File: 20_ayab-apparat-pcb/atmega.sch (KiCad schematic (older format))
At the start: 36 parts, among them P7 CONN_3X2, P8 CONN_4, P9 CONN_2, SW1 SW_PUSH, U6 ATMEGA32U4-A, U8 BLM21, X1 16MHz, X2 USBMICRO

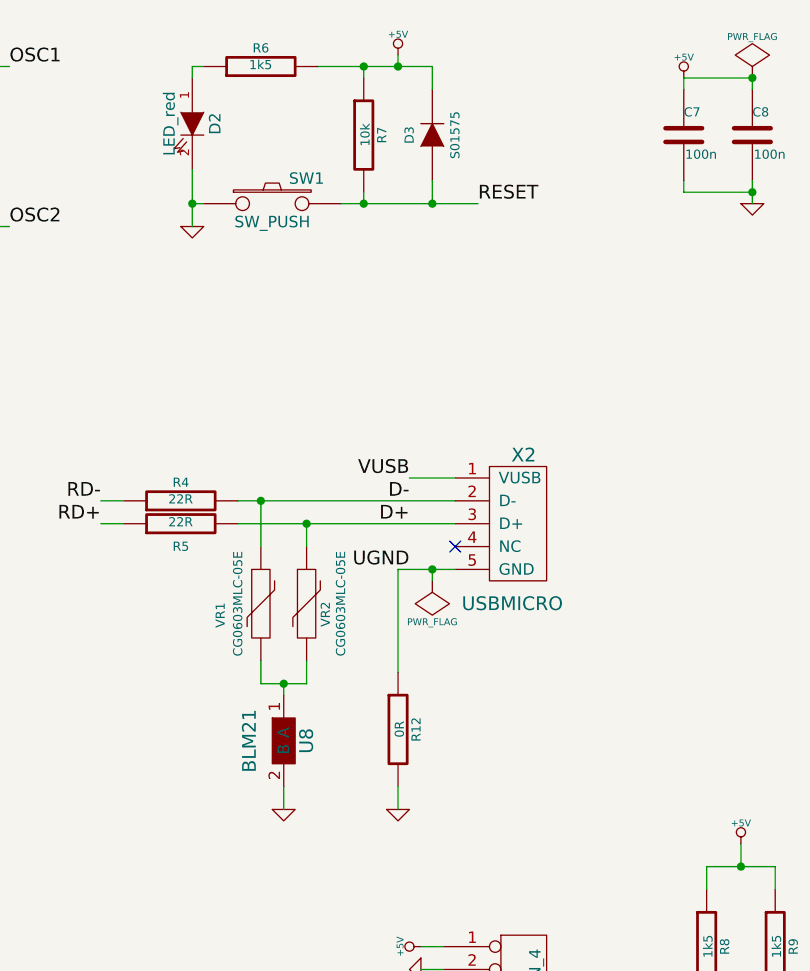
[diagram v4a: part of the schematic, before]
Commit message: BOM nearly done TODO add relais for autoswitch when USB 5V is connected to schematic
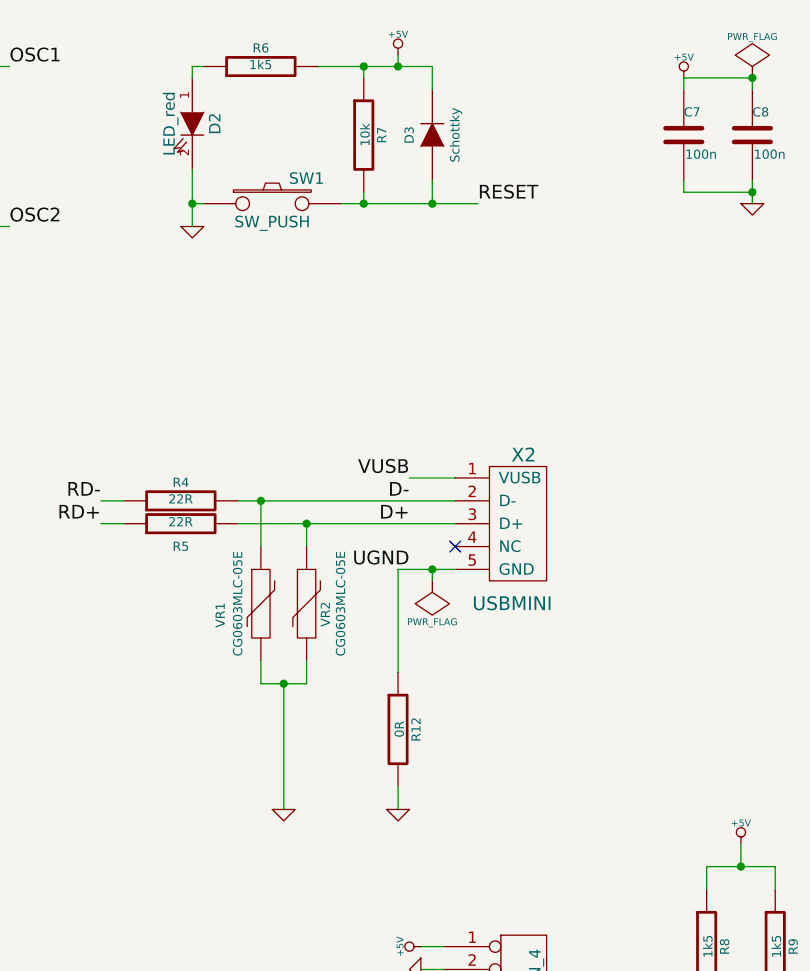
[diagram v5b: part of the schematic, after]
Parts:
- removed U8: BLM21, symbol FERRITE
- D3: value S01575 -> Schottky
- X2: value USBMICRO -> USBMINI
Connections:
- net GND: now also VR1.2, VR2.2
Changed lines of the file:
@@
 OSC2
 $Comp
-L GND #PWR034
+L GND #PWR033
 U 1 1 52E8074E
 P 4750 1850
-F 0 "#PWR034" H 4750 1850 30  0001 C CNN
+F 0 "#PWR033" H 4750 1850 30  0001 C CNN
 F 1 "GND" H 4750 1780 30  0001 C CNN
 F 2 "" H 4750 1850 60  0000 C CNN
@@
 $EndComp
 $Comp
-L PWR_FLAG #FLG035
+L PWR_FLAG #FLG034
 U 1 1 52E8077D
 P 4750 1100
-F 0 "#FLG035" H 4750 1195 30  0001 C CNN
+F 0 "#FLG034" H 4750 1195 30  0001 C CNN
 F 1 "PWR_FLAG" H 4750 1280 30  0000 C CNN
 F 2 "" H 4750 1100 60  0000 C CNN
@@
 $EndComp
 $Comp
-L GND #PWR036
+L GND #PWR035
 U 1 1 52E80927
 P 9200 1700
-F 0 "#PWR036" H 9200 1700 30  0001 C CNN
+F 0 "#PWR035" H 9200 1700 30  0001 C CNN
 F 1 "GND" H 9200 1630 30  0001 C CNN
 F 2 "" H 9200 1700 60  0000 C CNN
@@
 $EndComp
 $Comp
-L +5V #PWR037
+L +5V #PWR036
 U 1 1 52E8098A
 P 2650 2450
-F 0 "#PWR037" H 2650 2540 20  0001 C CNN
+F 0 "#PWR036" H 2650 2540 20  0001 C CNN
 F 1 "+5V" H 2650 2540 30  0000 C CNN
 F 2 "" H 2650 2450 60  0000 C CNN
@@
 $EndComp
 $Comp
-L PWR_FLAG #FLG038
+L PWR_FLAG #FLG037
 U 1 1 52E809A6
 P 9200 1150
-F 0 "#FLG038" H 9200 1245 30  0001 C CNN
+F 0 "#FLG037" H 9200 1245 30  0001 C CNN
 F 1 "PWR_FLAG" H 9200 1330 30  0000 C CNN
 F 2 "" H 9200 1150 60  0000 C CNN
@@
 $EndComp
 $Comp
-L GND #PWR039
+L GND #PWR038
 U 1 1 52E80AA1
 P 1450 5850
-F 0 "#PWR039" H 1450 5850 30  0001 C CNN
+F 0 "#PWR038" H 1450 5850 30  0001 C CNN
 F 1 "GND" H 1450 5780 30  0001 C CNN
 F 2 "" H 1450 5850 60  0000 C CNN
@@
 ISP
 $Comp
-L GND #PWR040
+L GND #PWR039
 U 1 1 52E80DFA
 P 7100 5850
-F 0 "#PWR040" H 7100 5850 30  0001 C CNN
+F 0 "#PWR039" H 7100 5850 30  0001 C CNN
 F 1 "GND" H 7100 5780 30  0001 C CNN
 F 2 "" H 7100 5850 60  0000 C CNN
@@
 MOSI
 $Comp
-L +5V #PWR041
+L +5V #PWR040
 U 1 1 52E80E45
 P 7100 5600
-F 0 "#PWR041" H 7100 5690 20  0001 C CNN
+F 0 "#PWR040" H 7100 5690 20  0001 C CNN
 F 1 "+5V" H 7100 5690 30  0000 C CNN
 F 2 "" H 7100 5600 60  0000 C CNN
@@
 P 7800 1400
 F 0 "D3" H 7800 1500 40  0000 C CNN
-F 1 "S01575" H 7800 1300 40  0000 C CNN
+F 1 "Schottky" H 7800 1300 40  0000 C CNN
 F 2 "" H 7800 1400 60  0000 C CNN
 F 3 "" H 7800 1400 60  0000 C CNN
@@
 $EndComp
 $Comp
-L +5V #PWR042
+L +5V #PWR041
 U 1 1 52E8110B
 P 7650 1050
-F 0 "#PWR042" H 7650 1140 20  0001 C CNN
+F 0 "#PWR041" H 7650 1140 20  0001 C CNN
 F 1 "+5V" H 7650 1140 30  0000 C CNN
 F 2 "" H 7650 1050 60  0000 C CNN
@@
 $EndComp
 $Comp
-L GND #PWR043
+L GND #PWR042
 U 1 1 52E813A7
 P 6750 1800
-F 0 "#PWR043" H 6750 1800 30  0001 C CNN
+F 0 "#PWR042" H 6750 1800 30  0001 C CNN
 F 1 "GND" H 6750 1730 30  0001 C CNN
 F 2 "" H 6750 1800 60  0000 C CNN
@@
 $EndComp
 $Comp
-L +5V #PWR044
+L +5V #PWR043
 U 1 1 52E81906
 P 4350 3500
-F 0 "#PWR044" H 4350 3590 20  0001 C CNN
+F 0 "#PWR043" H 4350 3590 20  0001 C CNN
 F 1 "+5V" H 4350 3590 30  0000 C CNN
 F 2 "" H 4350 3500 60  0000 C CNN
@@
 $EndComp
 $Comp
-L +5V #PWR045
+L +5V #PWR044
 U 1 1 52E81C3C
 P 1300 5300
-F 0 "#PWR045" H 1300 5390 20  0001 C CNN
+F 0 "#PWR044" H 1300 5390 20  0001 C CNN
 F 1 "+5V" H 1300 5390 30  0000 C CNN
 F 2 "" H 1300 5300 60  0000 C CNN
@@
 RESET
 $Comp
-L GND #PWR046
+L GND #PWR045
 U 1 1 52E9637A
 P 2900 6200
-F 0 "#PWR046" H 2900 6200 30  0001 C CNN
+F 0 "#PWR045" H 2900 6200 30  0001 C CNN
 F 1 "GND" H 2900 6130 30  0001 C CNN
 F 2 "" H 2900 6200 60  0000 C CNN
@@
 $EndComp
 $Comp
-L GND #PWR047
+L GND #PWR046
 U 1 1 52E97A05
 P 7150 4350
-F 0 "#PWR047" H 7150 4350 30  0001 C CNN
+F 0 "#PWR046" H 7150 4350 30  0001 C CNN
 F 1 "GND" H 7150 4280 30  0001 C CNN
 F 2 "" H 7150 4350 60  0000 C CNN
@@
 $EndComp
 $Comp
-L GND #PWR048
+L GND #PWR047
 U 1 1 52E97015
 P 10050 1700
-F 0 "#PWR048" H 10050 1700 30  0001 C CNN
+F 0 "#PWR047" H 10050 1700 30  0001 C CNN
 F 1 "GND" H 10050 1630 30  0001 C CNN
 F 2 "" H 10050 1700 60  0000 C CNN
@@
 $EndComp
 $Comp
-L GND #PWR049
+L GND #PWR048
 U 1 1 52E972FE
 P 10550 1700
-F 0 "#PWR049" H 10550 1700 30  0001 C CNN
+F 0 "#PWR048" H 10550 1700 30  0001 C CNN
 F 1 "GND" H 10550 1630 30  0001 C CNN
 F 2 "" H 10550 1700 60  0000 C CNN
@@
 RXLED
 $Comp
-L +5V #PWR050
+L +5V #PWR049
 U 1 1 52E980C3
 P 10050 4500
-F 0 "#PWR050" H 10050 4590 20  0001 C CNN
+F 0 "#PWR049" H 10050 4590 20  0001 C CNN
 F 1 "+5V" H 10050 4590 30  0000 C CNN
 F 2 "" H 10050 4500 60  0000 C CNN
@@
 $EndComp
 $Comp
-L +5V #PWR051
+L +5V #PWR050
 U 1 1 52EA92E6
 P 7750 5650
-F 0 "#PWR051" H 7750 5740 20  0001 C CNN
+F 0 "#PWR050" H 7750 5740 20  0001 C CNN
 F 1 "+5V" H 7750 5740 30  0000 C CNN
 F 2 "" H 7750 5650 60  0000 C CNN
@@
 $EndComp
 $Comp
-L +5V #PWR052
+L +5V #PWR051
 U 1 1 52EA9766
 P 7750 4950
-F 0 "#PWR052" H 7750 5040 20  0001 C CNN
+F 0 "#PWR051" H 7750 5040 20  0001 C CNN
 F 1 "+5V" H 7750 5040 30  0000 C CNN
 F 2 "" H 7750 4950 60  0000 C CNN
@@
 $EndComp
 $Comp
-L GND #PWR053
+L GND #PWR052
 U 1 1 52EA977A
 P 7750 5050
-F 0 "#PWR053" H 7750 5050 30  0001 C CNN
+F 0 "#PWR052" H 7750 5050 30  0001 C CNN
 F 1 "GND" H 7750 4980 30  0001 C CNN
 F 2 "" H 7750 5050 60  0000 C CNN
@@
 LED2
 $Comp
-L +5V #PWR054
+L +5V #PWR053
 U 1 1 52EA9B0A
 P 9150 4500
-F 0 "#PWR054" H 9150 4590 20  0001 C CNN
+F 0 "#PWR053" H 9150 4590 20  0001 C CNN
 F 1 "+5V" H 9150 4590 30  0000 C CNN
 F 2 "" H 9150 4500 60  0000 C CNN
@@
 LED1
 $Comp
-L +5V #PWR055
+L +5V #PWR054
 U 1 1 52EAA0EE
 P 3050 2050
-F 0 "#PWR055" H 3050 2140 20  0001 C CNN
+F 0 "#PWR054" H 3050 2140 20  0001 C CNN
 F 1 "+5V" H 3050 2140 30  0000 C CNN
 F 2 "" H 3050 2050 60  0000 C CNN
@@
 $EndComp
 $Comp
-L +5V #PWR056
+L +5V #PWR055
 U 1 1 52EAA124
 P 8900 1150
-F 0 "#PWR056" H 8900 1240 20  0001 C CNN
+F 0 "#PWR055" H 8900 1240 20  0001 C CNN
 F 1 "+5V" H 8900 1240 30  0000 C CNN
 F 2 "" H 8900 1150 60  0000 C CNN
@@
 P 8200 3100
 F 0 "X2" H 8200 2800 60  0000 C CNN
-F 1 "USBMICRO" H 8250 3450 60  0000 C CNN
+F 1 "USBMINI" H 8250 3450 60  0000 C CNN
 F 2 "" H 8200 3100 60  0000 C CNN
 F 3 "" H 8200 3100 60  0000 C CNN
 	1    8200 3100
 	-1   0    0    1
-$EndComp
-$Comp
-L FERRITE U8
-U 1 1 52EAB329
-P 7150 4050
-F 0 "U8" V 7250 4050 60  0000 C CNN
-F 1 "BLM21" V 7000 4050 60  0000 C CNN
-F 2 "" H 7150 4050 60  0000 C CNN
-F 3 "" H 7150 4050 60  0000 C CNN
-	1    7150 4050
-	1    0    0    -1
 $EndComp
 Text Notes 4150 7500 0    60   ~ 0
@@
 NoConn ~ 7900 3200
 $Comp
-L PWR_FLAG #FLG057
+L PWR_FLAG #FLG056
 U 1 1 52EECE5F
 P 3200 2600
-F 0 "#FLG057" H 3200 2695 30  0001 C CNN
+F 0 "#FLG056" H 3200 2695 30  0001 C CNN
 F 1 "PWR_FLAG" H 3200 2780 30  0000 C CNN
 F 2 "" H 3200 2600 60  0000 C CNN
@@
 $EndComp
 $Comp
-L PWR_FLAG #FLG058
+L PWR_FLAG #FLG057
 U 1 1 52EECE74
 P 7800 3350
-F 0 "#FLG058" H 7800 3445 30  0001 C CNN
+F 0 "#FLG057" H 7800 3445 30  0001 C CNN
 F 1 "PWR_FLAG" H 7800 3530 30  0000 C CNN
 F 2 "" H 7800 3350 60  0000 C CNN
@@
 	7050 3800 7050 3700
 Wire Wire Line
-	7150 4350 7150 4250
+	7150 3800 7150 4350
 Connection ~ 7150 3800
 Connection ~ 7250 3100
@@
 Wire Wire Line
 	7900 2900 7700 2900
-Wire Wire Line
-	7150 3800 7150 3850
 Wire Wire Line
 	3000 2600 3000 2700
@@
 	7650 3750 7650 3300
 $Comp
-L GND #PWR059
+L GND #PWR058
 U 1 1 52F17DE8
 P 7650 4350
-F 0 "#PWR059" H 7650 4350 30  0001 C CNN
+F 0 "#PWR058" H 7650 4350 30  0001 C CNN
 F 1 "GND" H 7650 4280 30  0001 C CNN
 F 2 "" H 7650 4350 60  0000 C CNN

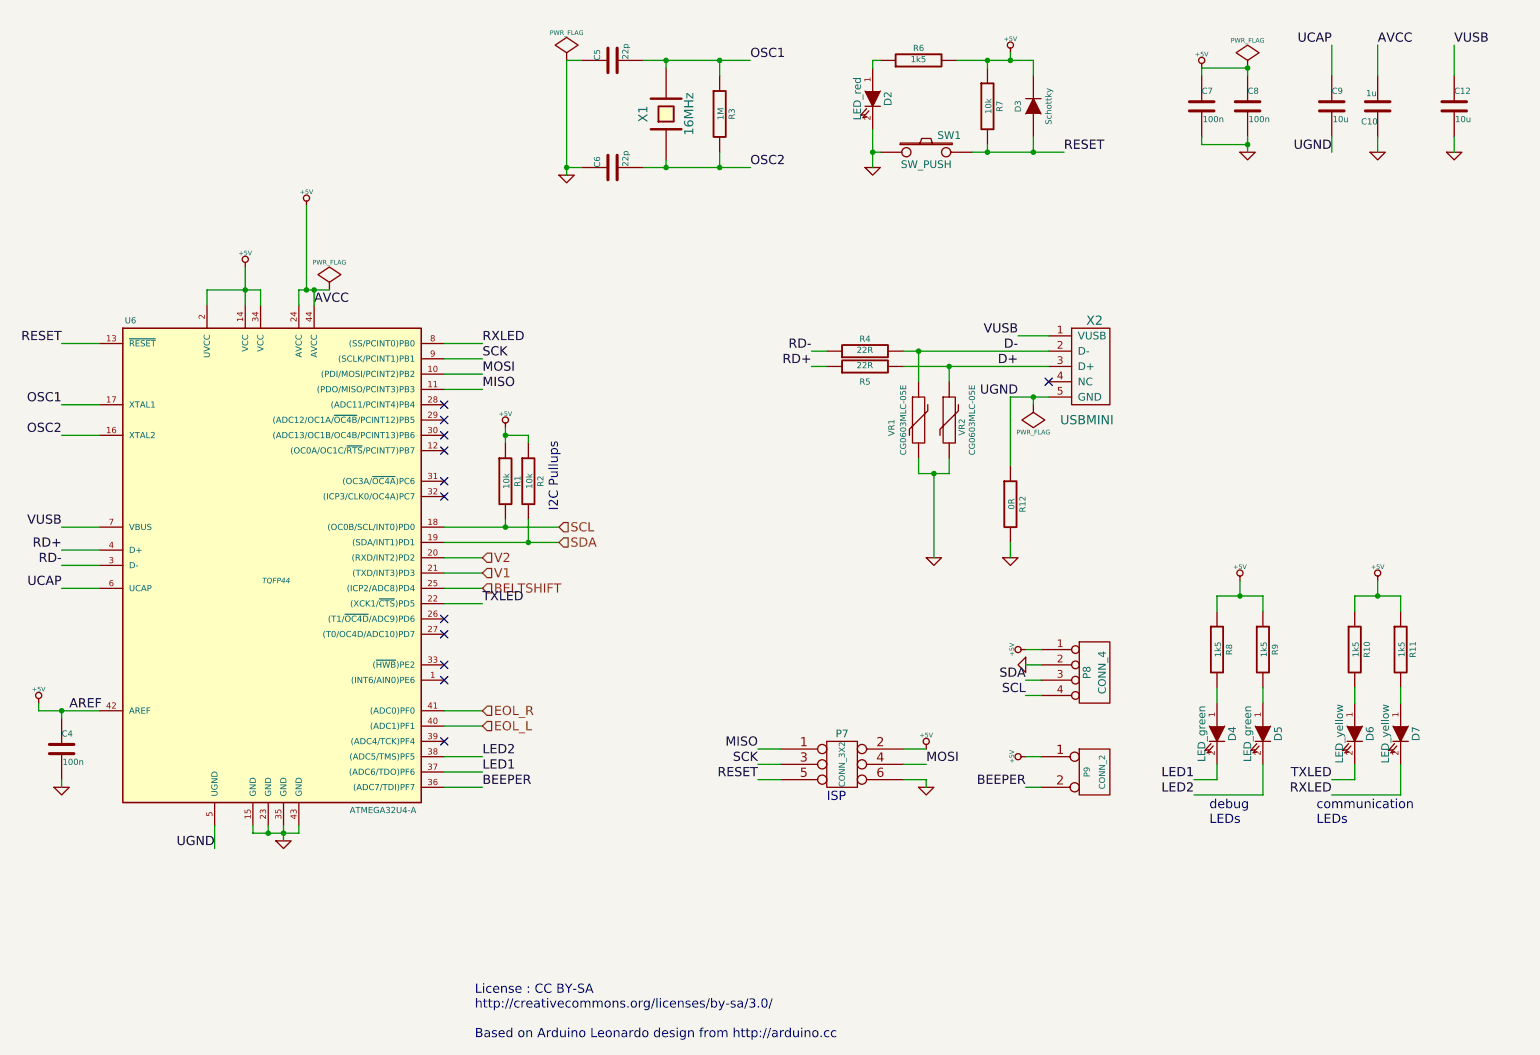
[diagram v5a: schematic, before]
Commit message: Added automatic switching between ATmega and original machine control when VUSB is attached
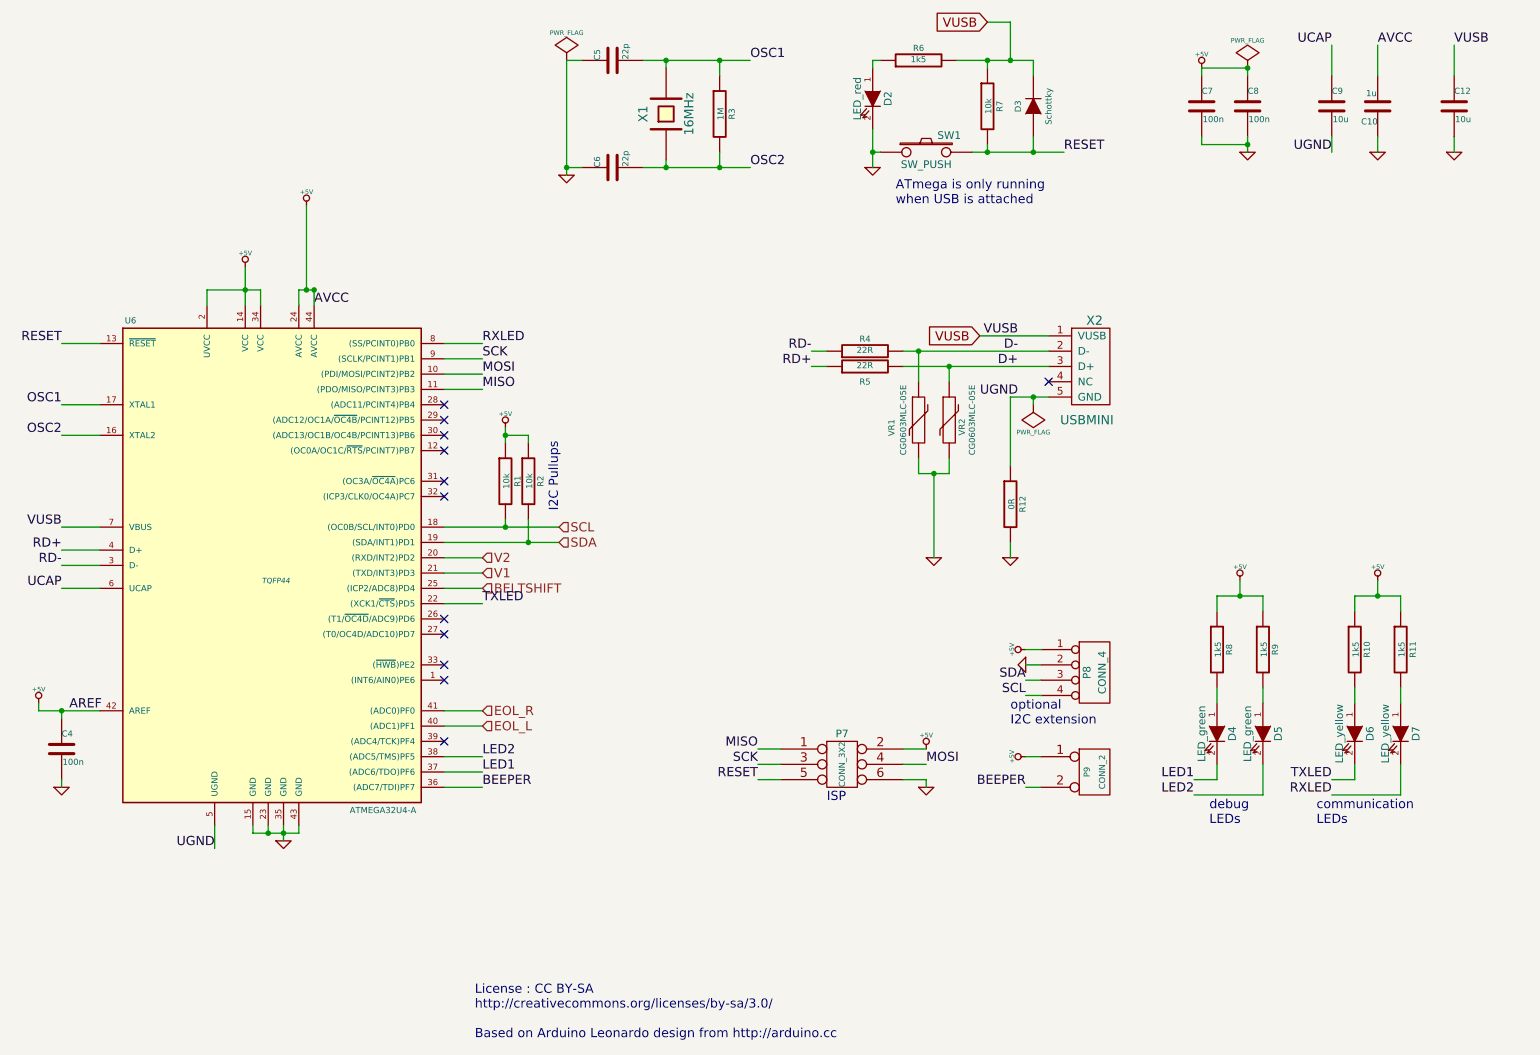
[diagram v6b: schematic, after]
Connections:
- net +5V: no longer D3.2 (K), R6.2, R7.1
- net VUSB: now also D3.2 (K), R6.2, R7.1
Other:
- note added: "ATmega is only running\nwhen USB is attached"
- note added: "optional\nI2C extension"
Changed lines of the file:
@@
 OSC2
 $Comp
-L GND #PWR033
+L GND #PWR034
 U 1 1 52E8074E
 P 4750 1850
-F 0 "#PWR033" H 4750 1850 30  0001 C CNN
+F 0 "#PWR034" H 4750 1850 30  0001 C CNN
 F 1 "GND" H 4750 1780 30  0001 C CNN
 F 2 "" H 4750 1850 60  0000 C CNN
@@
 $EndComp
 $Comp
-L PWR_FLAG #FLG034
+L PWR_FLAG #FLG035
 U 1 1 52E8077D
 P 4750 1100
-F 0 "#FLG034" H 4750 1195 30  0001 C CNN
+F 0 "#FLG035" H 4750 1195 30  0001 C CNN
 F 1 "PWR_FLAG" H 4750 1280 30  0000 C CNN
 F 2 "" H 4750 1100 60  0000 C CNN
@@
 $EndComp
 $Comp
-L GND #PWR035
+L GND #PWR036
 U 1 1 52E80927
 P 9200 1700
-F 0 "#PWR035" H 9200 1700 30  0001 C CNN
+F 0 "#PWR036" H 9200 1700 30  0001 C CNN
 F 1 "GND" H 9200 1630 30  0001 C CNN
 F 2 "" H 9200 1700 60  0000 C CNN
@@
 $EndComp
 $Comp
-L +5V #PWR036
+L +5V #PWR037
 U 1 1 52E8098A
 P 2650 2450
-F 0 "#PWR036" H 2650 2540 20  0001 C CNN
+F 0 "#PWR037" H 2650 2540 20  0001 C CNN
 F 1 "+5V" H 2650 2540 30  0000 C CNN
 F 2 "" H 2650 2450 60  0000 C CNN
@@
 $EndComp
 $Comp
-L PWR_FLAG #FLG037
+L PWR_FLAG #FLG038
 U 1 1 52E809A6
 P 9200 1150
-F 0 "#FLG037" H 9200 1245 30  0001 C CNN
+F 0 "#FLG038" H 9200 1245 30  0001 C CNN
 F 1 "PWR_FLAG" H 9200 1330 30  0000 C CNN
 F 2 "" H 9200 1150 60  0000 C CNN
@@
 $EndComp
 $Comp
-L GND #PWR038
+L GND #PWR039
 U 1 1 52E80AA1
 P 1450 5850
-F 0 "#PWR038" H 1450 5850 30  0001 C CNN
+F 0 "#PWR039" H 1450 5850 30  0001 C CNN
 F 1 "GND" H 1450 5780 30  0001 C CNN
 F 2 "" H 1450 5850 60  0000 C CNN
@@
 ISP
 $Comp
-L GND #PWR039
+L GND #PWR040
 U 1 1 52E80DFA
 P 7100 5850
-F 0 "#PWR039" H 7100 5850 30  0001 C CNN
+F 0 "#PWR040" H 7100 5850 30  0001 C CNN
 F 1 "GND" H 7100 5780 30  0001 C CNN
 F 2 "" H 7100 5850 60  0000 C CNN
@@
 MOSI
 $Comp
-L +5V #PWR040
+L +5V #PWR041
 U 1 1 52E80E45
 P 7100 5600
-F 0 "#PWR040" H 7100 5690 20  0001 C CNN
+F 0 "#PWR041" H 7100 5690 20  0001 C CNN
 F 1 "+5V" H 7100 5690 30  0000 C CNN
 F 2 "" H 7100 5600 60  0000 C CNN
@@
 	1    7800 1400
 	0    -1   -1   0
-$EndComp
-$Comp
-L +5V #PWR041
-U 1 1 52E8110B
-P 7650 1050
-F 0 "#PWR041" H 7650 1140 20  0001 C CNN
-F 1 "+5V" H 7650 1140 30  0000 C CNN
-F 2 "" H 7650 1050 60  0000 C CNN
-F 3 "" H 7650 1050 60  0000 C CNN
-	1    7650 1050
-	1    0    0    -1
 $EndComp
 Text Label 8000 1700 0    60   ~ 0
@@
 $Comp
 L PWR_FLAG #FLG056
-U 1 1 52EECE5F
-P 3200 2600
-F 0 "#FLG056" H 3200 2695 30  0001 C CNN
-F 1 "PWR_FLAG" H 3200 2780 30  0000 C CNN
-F 2 "" H 3200 2600 60  0000 C CNN
-F 3 "" H 3200 2600 60  0000 C CNN
-	1    3200 2600
-	1    0    0    -1
-$EndComp
-$Comp
-L PWR_FLAG #FLG057
 U 1 1 52EECE74
 P 7800 3350
-F 0 "#FLG057" H 7800 3445 30  0001 C CNN
+F 0 "#FLG056" H 7800 3445 30  0001 C CNN
 F 1 "PWR_FLAG" H 7800 3530 30  0000 C CNN
 F 2 "" H 7800 3350 60  0000 C CNN
@@
 	7800 1100 7800 1200
 Wire Wire Line
-	7650 1100 7650 1050
+	7650 850  7650 1100
 Connection ~ 7650 1100
 Wire Wire Line
@@
 	10050 1600 10050 1700
 Wire Wire Line
-	3000 2600 3200 2600
-Wire Wire Line
 	10550 1600 10550 1700
 Wire Wire Line
@@
 	9300 5900 8850 5900
 Wire Wire Line
-	7900 2900 7700 2900
+	7900 2900 7450 2900
 Wire Wire Line
 	3000 2600 3000 2700
@@
 	7650 3750 7650 3300
 $Comp
-L GND #PWR058
+L GND #PWR057
 U 1 1 52F17DE8
 P 7650 4350
-F 0 "#PWR058" H 7650 4350 30  0001 C CNN
+F 0 "#PWR057" H 7650 4350 30  0001 C CNN
 F 1 "GND" H 7650 4280 30  0001 C CNN
 F 2 "" H 7650 4350 60  0000 C CNN
@@
 Wire Wire Line
 	7650 4250 7650 4350
+Text GLabel 7450 2900 0    60   Input ~ 0
+VUSB
+Wire Wire Line
+	3000 2600 3100 2600
+Text GLabel 7500 850  0    60   Input ~ 0
+VUSB
+Wire Wire Line
+	7500 850  7650 850
+Text Notes 6900 2050 0    60   ~ 0
+ATmega is only running\nwhen USB is attached
+Text Notes 7650 5450 0    60   ~ 0
+optional\nI2C extension
 $EndSCHEMATC
